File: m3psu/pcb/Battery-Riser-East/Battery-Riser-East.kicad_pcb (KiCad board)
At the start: 2 copper layers, 20 x 68 mm, 2 parts, among them J1 EAST TOP, J2 EAST BOT

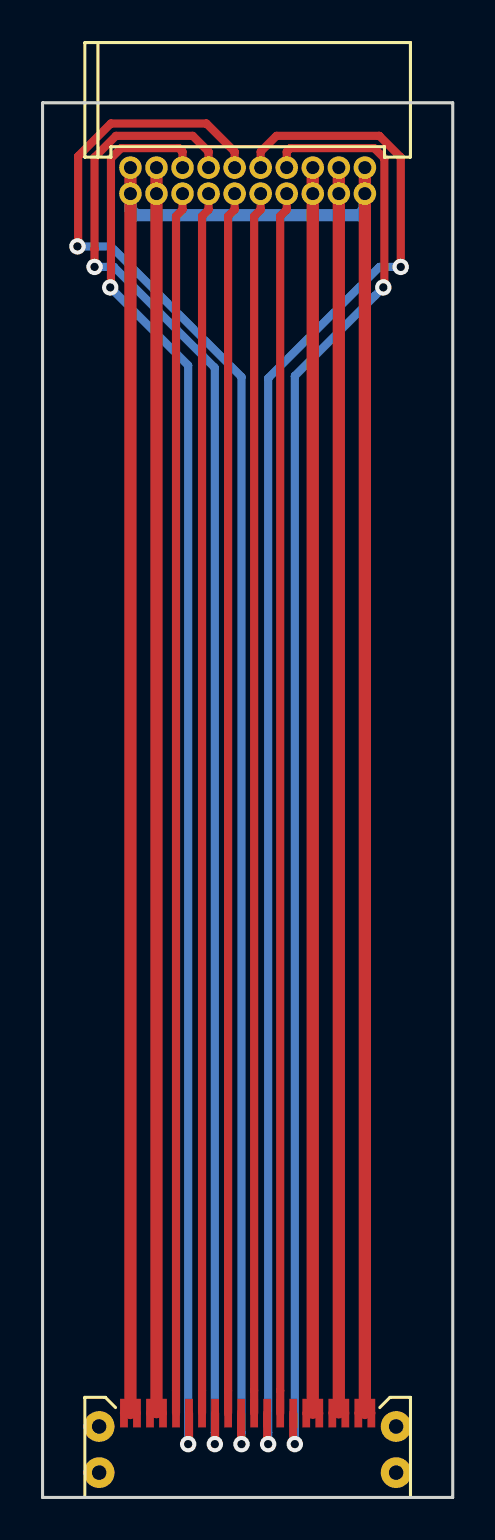
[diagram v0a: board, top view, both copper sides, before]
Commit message: Fix trace widths and spacing on riser boards
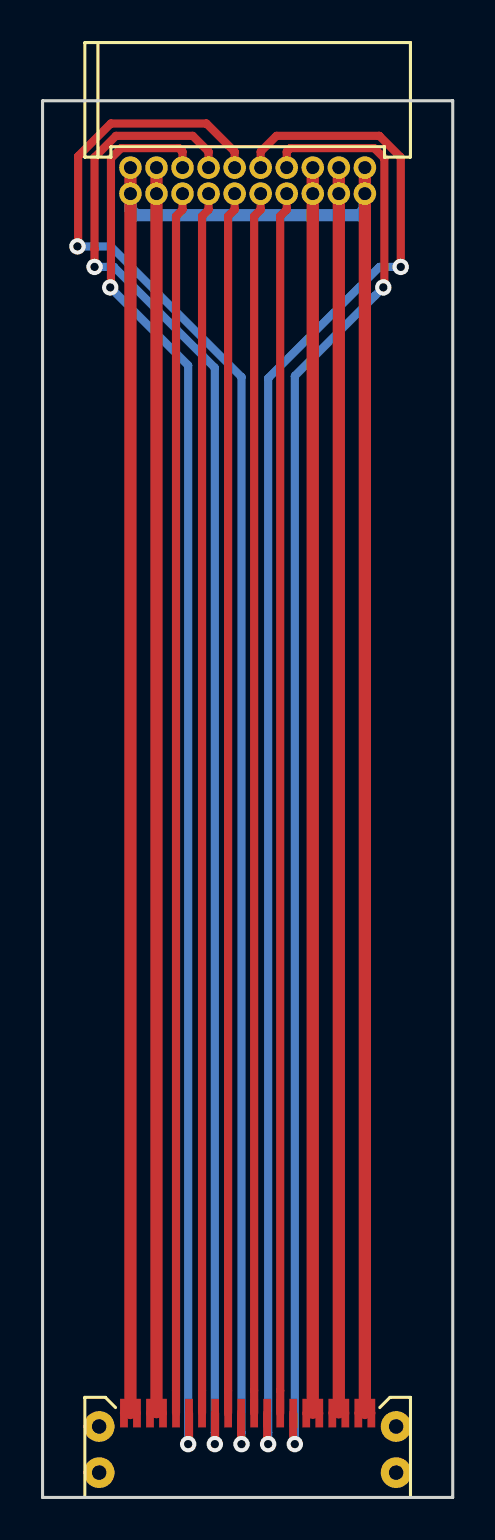
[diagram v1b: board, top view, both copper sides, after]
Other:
- board size 20 x 68 mm -> 20 x 68.1 mm
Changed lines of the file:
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@@
   (general
     (links 26)
-    (no_connects 26)
-    (area 139.924999 41.924999 160.075001 115.455001)
+    (no_connects 0)
+    (area 145.875 58.594999 166.075001 135.405001)
     (thickness 1.6)
     (drawings 4)
@@
   )
   (setup
-    (last_trace_width 0.4)
+    (last_trace_width 0.25)
     (user_trace_width 0.2)
     (user_trace_width 0.25)
@@
   )
   (gr_line (start 166 130) (end 146 130) (layer Edge.Cuts) (width 0.15))
-  (gr_line (start 166 62) (end 166 130) (layer Edge.Cuts) (width 0.15))
-  (gr_line (start 146 62) (end 166 62) (layer Edge.Cuts) (width 0.15))
-  (gr_line (start 146 130) (end 146 62) (layer Edge.Cuts) (width 0.15))
+  (gr_line (start 166 61.9) (end 166 130) (layer Edge.Cuts) (width 0.15))
+  (gr_line (start 146 61.9) (end 166 61.9) (layer Edge.Cuts) (width 0.15))
+  (gr_line (start 146 130) (end 146 61.9) (layer Edge.Cuts) (width 0.15))
   (segment (start 162.0325 125.89) (end 161.71 125.89) (width 0.4) (layer F.Cu) (net 1))
   (segment (start 161.3975 125.89) (end 161.71 125.89) (width 0.4) (layer F.Cu) (net 1))

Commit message: Widen tracks, add logo, fix DRC errors in East riser.
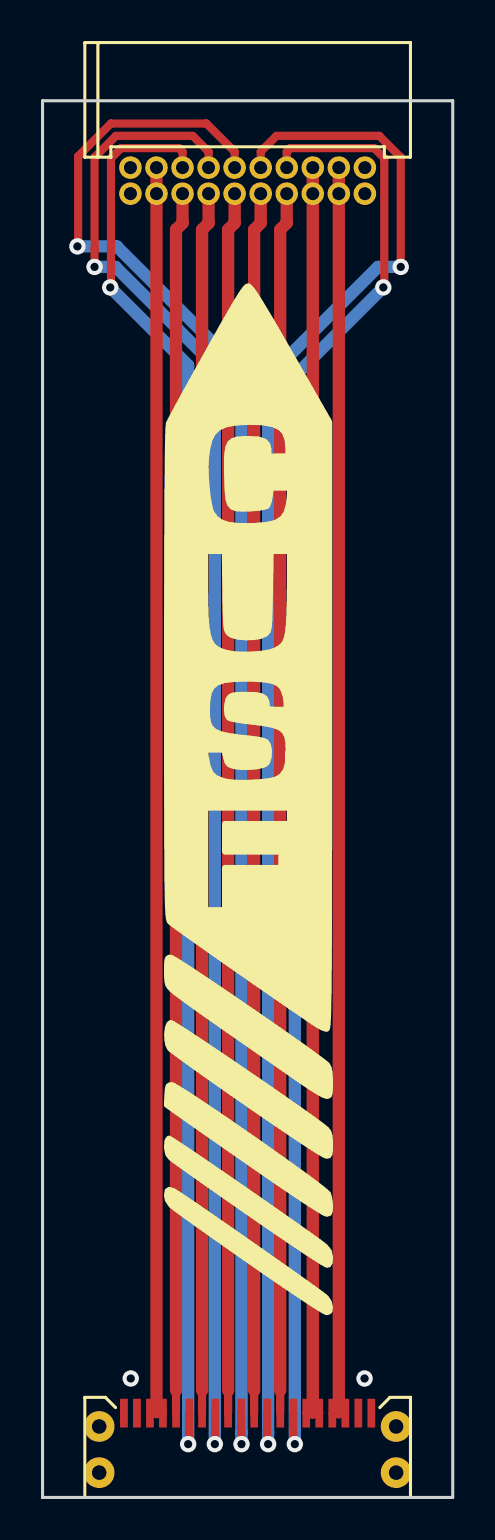
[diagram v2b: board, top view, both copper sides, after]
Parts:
- added G***: LOGO, m3psu:cusf_logo_large, F.Cu at (156.0, 96.0)
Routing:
- net GND: track 135.9 -> 0.00 mm
- net (no net): vias 0 -> 2
- added copper zone on B.Cu, net GND
- added copper zone on F.Cu, net GND
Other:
- net class Default: clearance 0.2 -> 0.15
- rule trace_clearance: 0.2 -> 0.15

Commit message: fix riser ground pour, stitching, silk, mask clearance, generate gerbers
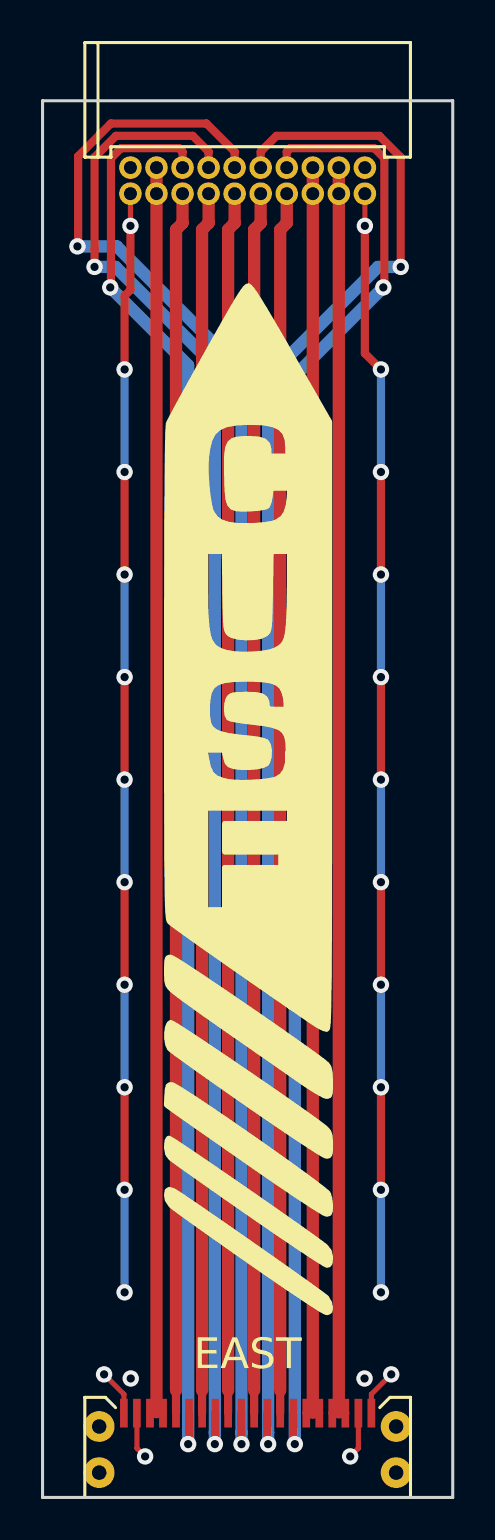
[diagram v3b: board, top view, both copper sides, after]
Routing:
- net GND: track 0.00 -> 116.7 mm, vias 0 -> 26
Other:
- rule pad_to_mask_clearance: 0.2 -> 0
- board text added: "EAST"
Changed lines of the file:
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@@
-(kicad_pcb (version 4) (host pcbnew 4.0.0-rc2-stable)
+(kicad_pcb (version 4) (host pcbnew 4.1.0-alpha+201605071002+6776~44~ubuntu14.04.1-product)
   (general
     (links 26)
     (no_connects 0)
-    (area 145.875 58.594999 166.075001 135.405001)
+    (area 145.924999 58.644999 166.075001 135.355001)
     (thickness 1.6)
-    (drawings 4)
-    (tracks 102)
+    (drawings 5)
+    (tracks 161)
     (zones 0)
     (modules 3)
@@
   )
   (setup
-    (last_trace_width 0.6)
+    (last_trace_width 0.25)
     (user_trace_width 0.2)
     (user_trace_width 0.25)
@@
     (user_trace_width 0.8)
     (trace_clearance 0.15)
-    (zone_clearance 0.2)
+    (zone_clearance 0.3)
     (zone_45_only no)
     (trace_min 0.2)
@@
     (pad_size 1.524 1.524)
     (pad_drill 0.762)
-    (pad_to_mask_clearance 0.2)
+    (pad_to_mask_clearance 0)
     (aux_axis_origin 0 0)
     (visible_elements 7FFFFFFF)
     (pcbplotparams
-      (layerselection 0x00030_80000001)
-      (usegerberextensions false)
+      (layerselection 0x010f0_ffffffff)
+      (usegerberextensions true)
       (excludeedgelayer true)
       (linewidth 0.100000)
@@
       (hpglpenspeed 20)
       (hpglpendiameter 15)
-      (hpglpenoverlay 2)
       (psnegative false)
       (psa4output false)
-      (plotreference true)
-      (plotvalue true)
+      (plotreference false)
+      (plotvalue false)
       (plotinvisibletext false)
       (padsonsilk false)
-      (subtractmaskfromsilk false)
+      (subtractmaskfromsilk true)
       (outputformat 1)
       (mirror false)
-      (drillshape 1)
+      (drillshape 0)
       (scaleselection 1)
-      (outputdirectory ""))
+      (outputdirectory gerbers/))
   )
   (net 0 "")
@@
   (module agg:SFM-110-02-L-DH (layer F.Cu)
     (at 156 129.7 180)
-    (fp_text reference J2 (at 9 2.5 450) (layer F.Fab)
+    (fp_text reference J2 (at 9 2.5 90) (layer F.Fab)
       (effects (font (size 1 1) (thickness 0.15)))
     )
@@
   (module agg:TFML-110-01-L-D-RA (layer F.Cu)
     (at 156 63 180)
-    (fp_text reference J1 (at 9 -0.859 450) (layer F.Fab)
+    (fp_text reference J1 (at 9 -0.859 90) (layer F.Fab)
       (effects (font (size 1 1) (thickness 0.15)))
     )
@@
       (xy 3.986213 -3.606549) (xy 3.986213 -3.606549)) (layer F.SilkS) (width 0.27))
   )
+  (gr_text EAST (at 156 123) (layer F.SilkS)
+    (effects (font (size 1.5 1.5) (thickness 0.3)))
+  )
   (gr_line (start 166 130) (end 146 130) (layer Edge.Cuts) (width 0.15))
   (gr_line (start 166 61.9) (end 166 130) (layer Edge.Cuts) (width 0.15))
@@
   (via (at 150.3 124.2) (size 0.8) (drill 0.4) (layers F.Cu B.Cu) (net 0))
   (via (at 161.7 124.2) (size 0.8) (drill 0.4) (layers F.Cu B.Cu) (net 0))
+  (segment (start 161.715 68) (end 161.715 74.215) (width 0.4) (layer F.Cu) (net 1))
+  (via (at 161.715 68) (size 0.8) (drill 0.4) (layers F.Cu B.Cu) (net 1))
+  (segment (start 161.715 66.429) (end 161.715 68) (width 0.25) (layer F.Cu) (net 1))
+  (segment (start 150.285 68) (end 150.285 71.125002) (width 0.4) (layer F.Cu) (net 1))
+  (segment (start 150.285 66.429) (end 150.285 68) (width 0.25) (layer F.Cu) (net 1))
+  (via (at 150.285 68) (size 0.8) (drill 0.4) (layers F.Cu B.Cu) (net 1))
+  (segment (start 161.3975 125.89) (end 161.3975 127.6025) (width 0.25) (layer F.Cu) (net 1))
+  (segment (start 161.3975 127.6025) (end 161 128) (width 0.25) (layer F.Cu) (net 1))
+  (via (at 161 128) (size 0.8) (drill 0.4) (layers F.Cu B.Cu) (net 1))
+  (segment (start 150.6025 125.89) (end 150.6025 127.6025) (width 0.25) (layer F.Cu) (net 1))
+  (segment (start 150.6025 127.6025) (end 151 128) (width 0.25) (layer F.Cu) (net 1))
+  (via (at 151 128) (size 0.8) (drill 0.4) (layers F.Cu B.Cu) (net 1))
+  (segment (start 162.0325 125.89) (end 162.0325 124.9675) (width 0.25) (layer F.Cu) (net 1))
+  (segment (start 162.0325 124.9675) (end 163 124) (width 0.25) (layer F.Cu) (net 1))
+  (via (at 163 124) (size 0.8) (drill 0.4) (layers F.Cu B.Cu) (net 1))
+  (segment (start 149.9675 125.89) (end 149.9675 124.9675) (width 0.25) (layer F.Cu) (net 1))
+  (segment (start 149.9675 124.9675) (end 149 124) (width 0.25) (layer F.Cu) (net 1))
+  (via (at 149 124) (size 0.8) (drill 0.4) (layers F.Cu B.Cu) (net 1))
+  (segment (start 162.5 115) (end 162.5 120) (width 0.4) (layer B.Cu) (net 1))
+  (via (at 162.5 120) (size 0.8) (drill 0.4) (layers F.Cu B.Cu) (net 1))
+  (segment (start 162.5 110) (end 162.5 115) (width 0.4) (layer F.Cu) (net 1))
+  (via (at 162.5 115) (size 0.8) (drill 0.4) (layers F.Cu B.Cu) (net 1))
+  (segment (start 162.5 105) (end 162.5 110) (width 0.4) (layer B.Cu) (net 1))
+  (via (at 162.5 110) (size 0.8) (drill 0.4) (layers F.Cu B.Cu) (net 1))
+  (segment (start 162.5 100) (end 162.5 105) (width 0.4) (layer F.Cu) (net 1))
+  (via (at 162.5 105) (size 0.8) (drill 0.4) (layers F.Cu B.Cu) (net 1))
+  (segment (start 162.5 95) (end 162.5 100) (width 0.4) (layer B.Cu) (net 1))
+  (via (at 162.5 100) (size 0.8) (drill 0.4) (layers F.Cu B.Cu) (net 1))
+  (segment (start 162.5 90) (end 162.5 95) (width 0.4) (layer F.Cu) (net 1))
+  (via (at 162.5 95) (size 0.8) (drill 0.4) (layers F.Cu B.Cu) (net 1))
+  (segment (start 162.5 85) (end 162.5 90) (width 0.4) (layer B.Cu) (net 1))
+  (via (at 162.5 90) (size 0.8) (drill 0.4) (layers F.Cu B.Cu) (net 1))
+  (segment (start 162.5 80) (end 162.5 85) (width 0.4) (layer F.Cu) (net 1))
+  (via (at 162.5 85) (size 0.8) (drill 0.4) (layers F.Cu B.Cu) (net 1))
+  (segment (start 162.5 75) (end 162.5 80) (width 0.4) (layer B.Cu) (net 1))
+  (via (at 162.5 80) (size 0.8) (drill 0.4) (layers F.Cu B.Cu) (net 1))
+  (segment (start 161.715 74.215) (end 162.5 75) (width 0.4) (layer F.Cu) (net 1))
+  (via (at 162.5 75) (size 0.8) (drill 0.4) (layers F.Cu B.Cu) (net 1))
+  (segment (start 150 115) (end 150 120) (width 0.4) (layer B.Cu) (net 1))
+  (via (at 150 120) (size 0.8) (drill 0.4) (layers F.Cu B.Cu) (net 1))
+  (segment (start 150 110) (end 150 115) (width 0.4) (layer F.Cu) (net 1))
+  (via (at 150 115) (size 0.8) (drill 0.4) (layers F.Cu B.Cu) (net 1))
+  (segment (start 150 105) (end 150 110) (width 0.4) (layer B.Cu) (net 1))
+  (via (at 150 110) (size 0.8) (drill 0.4) (layers F.Cu B.Cu) (net 1))
+  (segment (start 150 100) (end 150 105) (width 0.4) (layer F.Cu) (net 1))
+  (via (at 150 105) (size 0.8) (drill 0.4) (layers F.Cu B.Cu) (net 1))
+  (segment (start 150 95) (end 150 100) (width 0.4) (layer B.Cu) (net 1))
+  (via (at 150 100) (size 0.8) (drill 0.4) (layers F.Cu B.Cu) (net 1))
+  (segment (start 150 90) (end 150 95) (width 0.4) (layer F.Cu) (net 1))
+  (via (at 150 95) (size 0.8) (drill 0.4) (layers F.Cu B.Cu) (net 1))
+  (segment (start 150 85) (end 150 90) (width 0.4) (layer B.Cu) (net 1))
+  (via (at 150 90) (size 0.8) (drill 0.4) (layers F.Cu B.Cu) (net 1))
+  (segment (start 150 80) (end 150 85) (width 0.4) (layer F.Cu) (net 1))
+  (via (at 150 85) (size 0.8) (drill 0.4) (layers F.Cu B.Cu) (net 1))
+  (segment (start 150 75) (end 150 80) (width 0.4) (layer B.Cu) (net 1))
+  (via (at 150 80) (size 0.8) (drill 0.4) (layers F.Cu B.Cu) (net 1))
+  (segment (start 150 71.410002) (end 150 75) (width 0.4) (layer F.Cu) (net 1))
+  (via (at 150 75) (size 0.8) (drill 0.4) (layers F.Cu B.Cu) (net 1))
+  (segment (start 150.285 71.125002) (end 150 71.410002) (width 0.4) (layer F.Cu) (net 1))
   (segment (start 160.7625 125.89) (end 160.41 125.89) (width 0.4) (layer F.Cu) (net 2))
   (segment (start 160.1275 125.89) (end 160.41 125.89) (width 0.4) (layer F.Cu) (net 2))
@@
   )
   (zone (net 1) (net_name GND) (layer B.Cu) (hatch edge 0.508)
-    (connect_pads (clearance 0.2))
+    (connect_pads (clearance 0.3))
     (min_thickness 0.2)
     (fill yes (arc_segments 16) (thermal_gap 0.15) (thermal_bridge_width 0.3))
